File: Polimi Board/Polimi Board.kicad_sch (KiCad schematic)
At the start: 15 parts, among them J1 Conn_01x04_Socket, J2 USB_B_Micro, U1 STM32F205RCTx, U2 FT2232D, U3 LAN8742A, Y1 8MHz

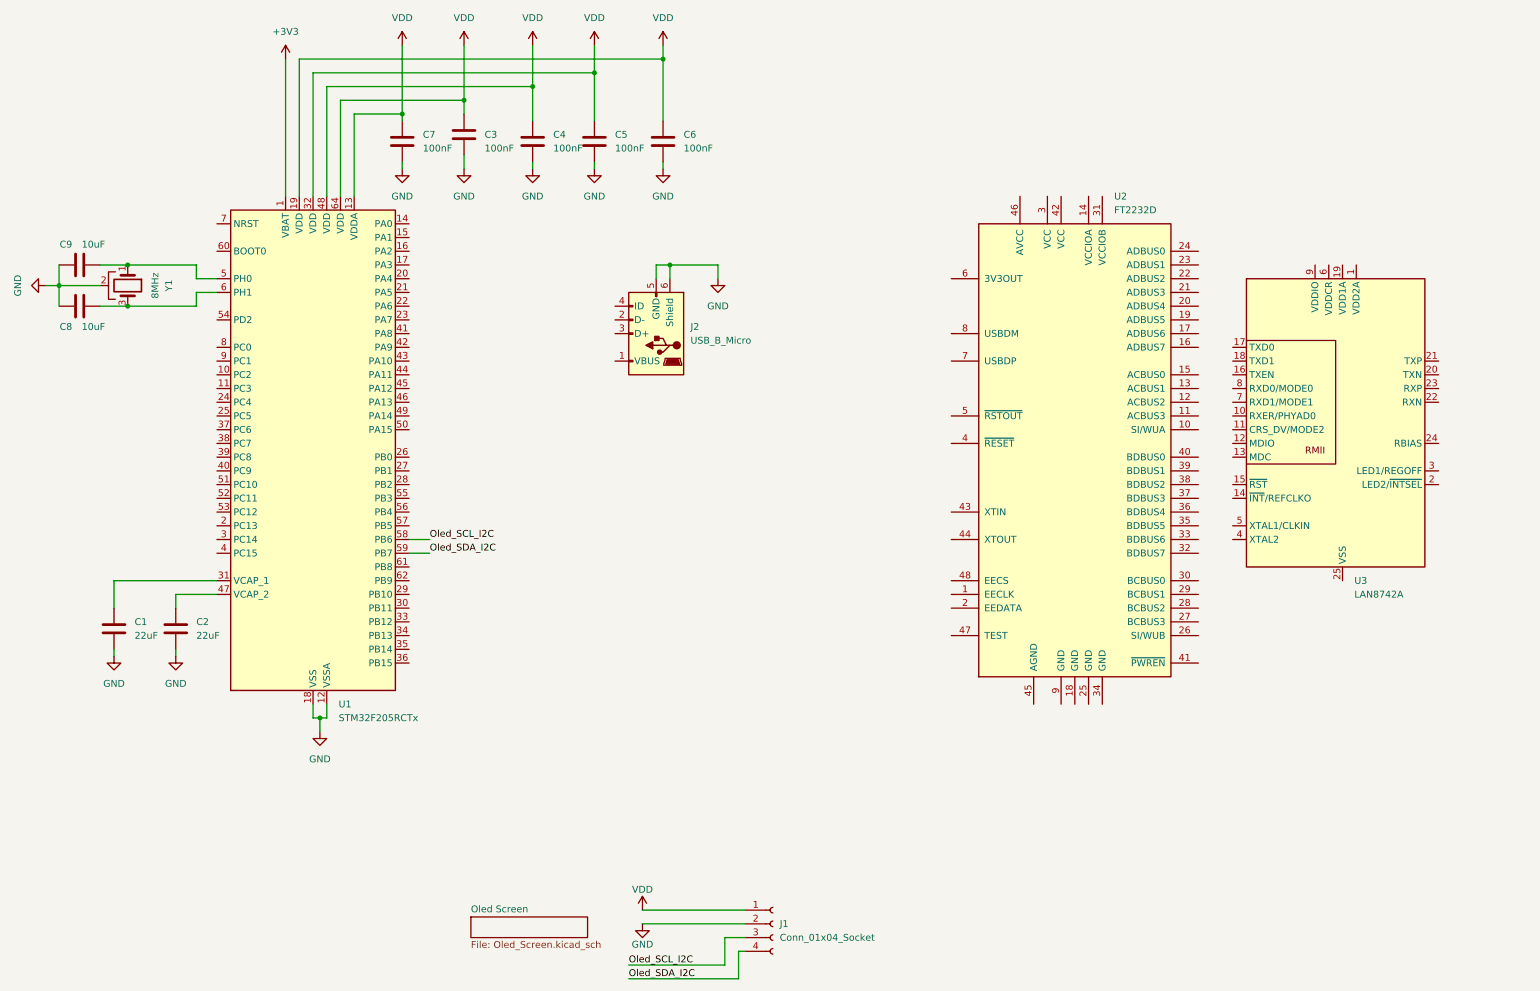
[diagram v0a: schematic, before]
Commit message: added programming oled and SD
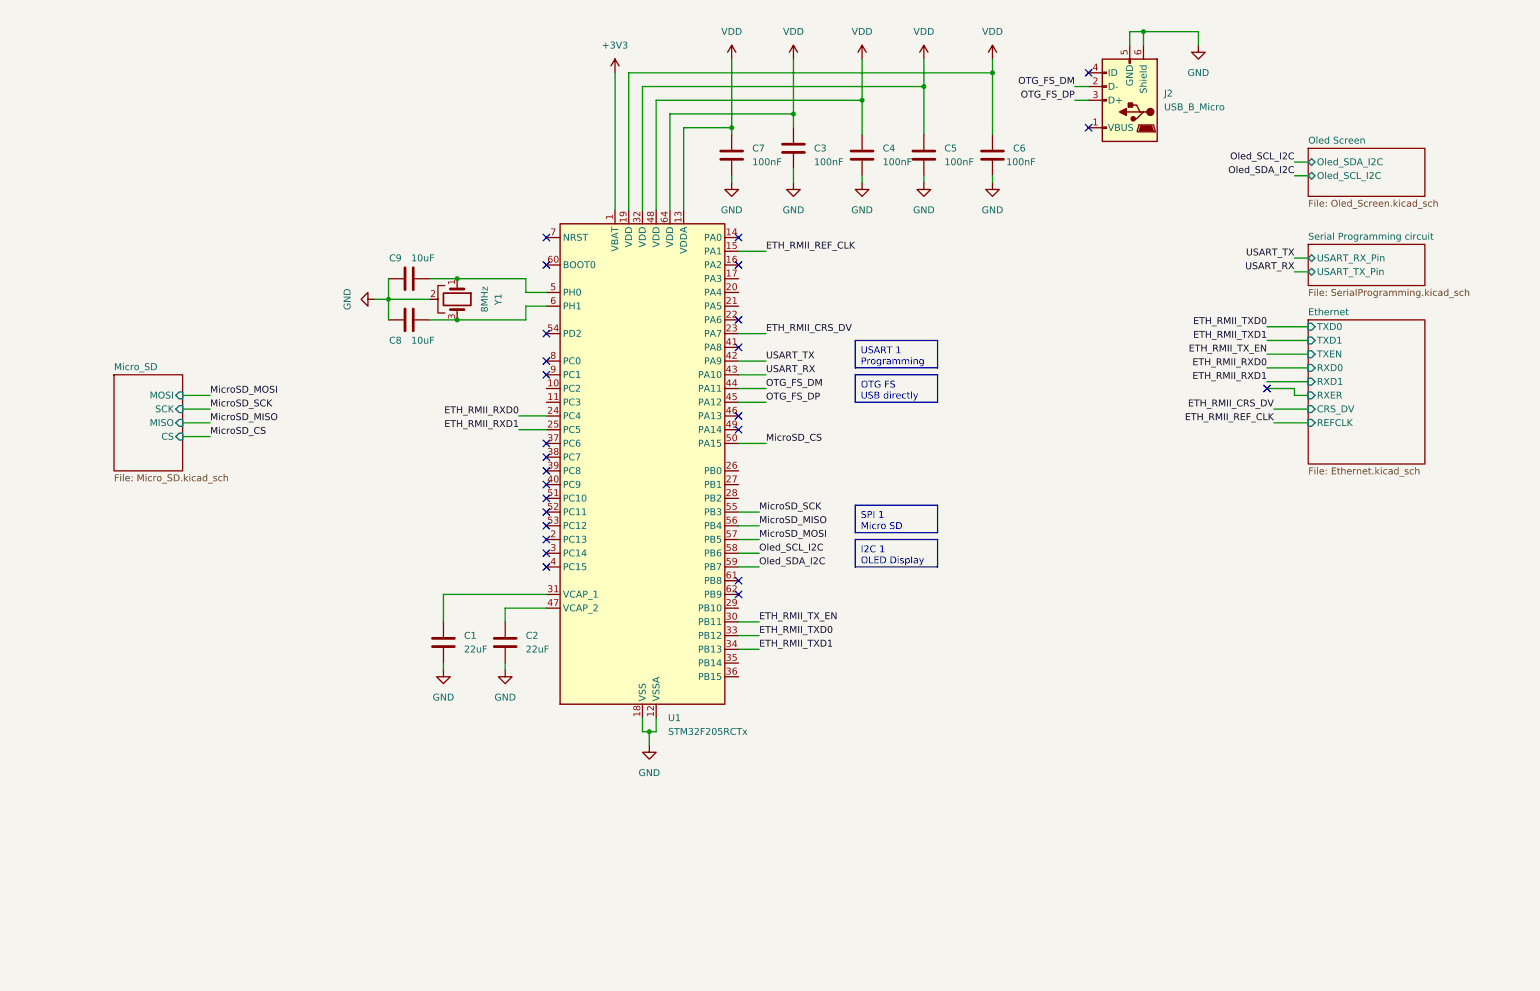
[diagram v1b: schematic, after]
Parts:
- removed J1: Conn_01x04_Socket, symbol Connector:Conn_01x04_Socket
- removed U2: FT2232D, Package_QFP:LQFP-48_7x7mm_P0.5mm, symbol Interface_USB:FT2232D
- removed U3: LAN8742A, Package_DFN_QFN:VQFN-24-1EP_4x4mm_P0.5mm_EP2.5x2.5mm_ThermalVias, symbol Interface_Ethernet:LAN8742A
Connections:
- net OTG_FS_DM: now reaches J2.2 (D-)
- net OTG_FS_DM: now also U1.44 (PA11)
- net OTG_FS_DP: now reaches J2.3 (D+)
- net OTG_FS_DP: now also U1.45 (PA12)
- net ETH_RMII_REF_CLK: now reaches U1.15 (PA1)
- net ETH_RMII_CRS_DV: now reaches U1.23 (PA7)
- net ETH_RMII_RXD0: now reaches U1.24 (PC4)
- net ETH_RMII_RXD1: now reaches U1.25 (PC5)
- net ETH_RMII_TX_EN: now reaches U1.30 (PB11)
- net ETH_RMII_TXD0: now reaches U1.33 (PB12)
- net ETH_RMII_TXD1: now reaches U1.34 (PB13)
- net USART_TX: now reaches U1.42 (PA9)
- net USART_RX: now reaches U1.43 (PA10)
- net MicroSD_CS: now reaches U1.50 (PA15)
- net MicroSD_SCK: now reaches U1.55 (PB3)
- net MicroSD_MISO: now reaches U1.56 (PB4)
- net MicroSD_MOSI: now reaches U1.57 (PB5)
- no-connect marks 0 -> 26
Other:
- added sheet Ethernet (Ethernet.kicad_sch)
- added sheet Micro_SD (Micro_SD.kicad_sch)
- added sheet Serial Programming circuit (SerialProgramming.kicad_sch)
- sheet Oled Screen ports: added Oled_SCL_I2C, Oled_SDA_I2C; removed none
- title: Polimi Board - Embedded Systems project -> Polimi Board 
- moved on the sheet: C1, C2, C3, C4, C5, C6, C7, C8, C9, J2, U1, Y1

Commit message: Added GPIOs
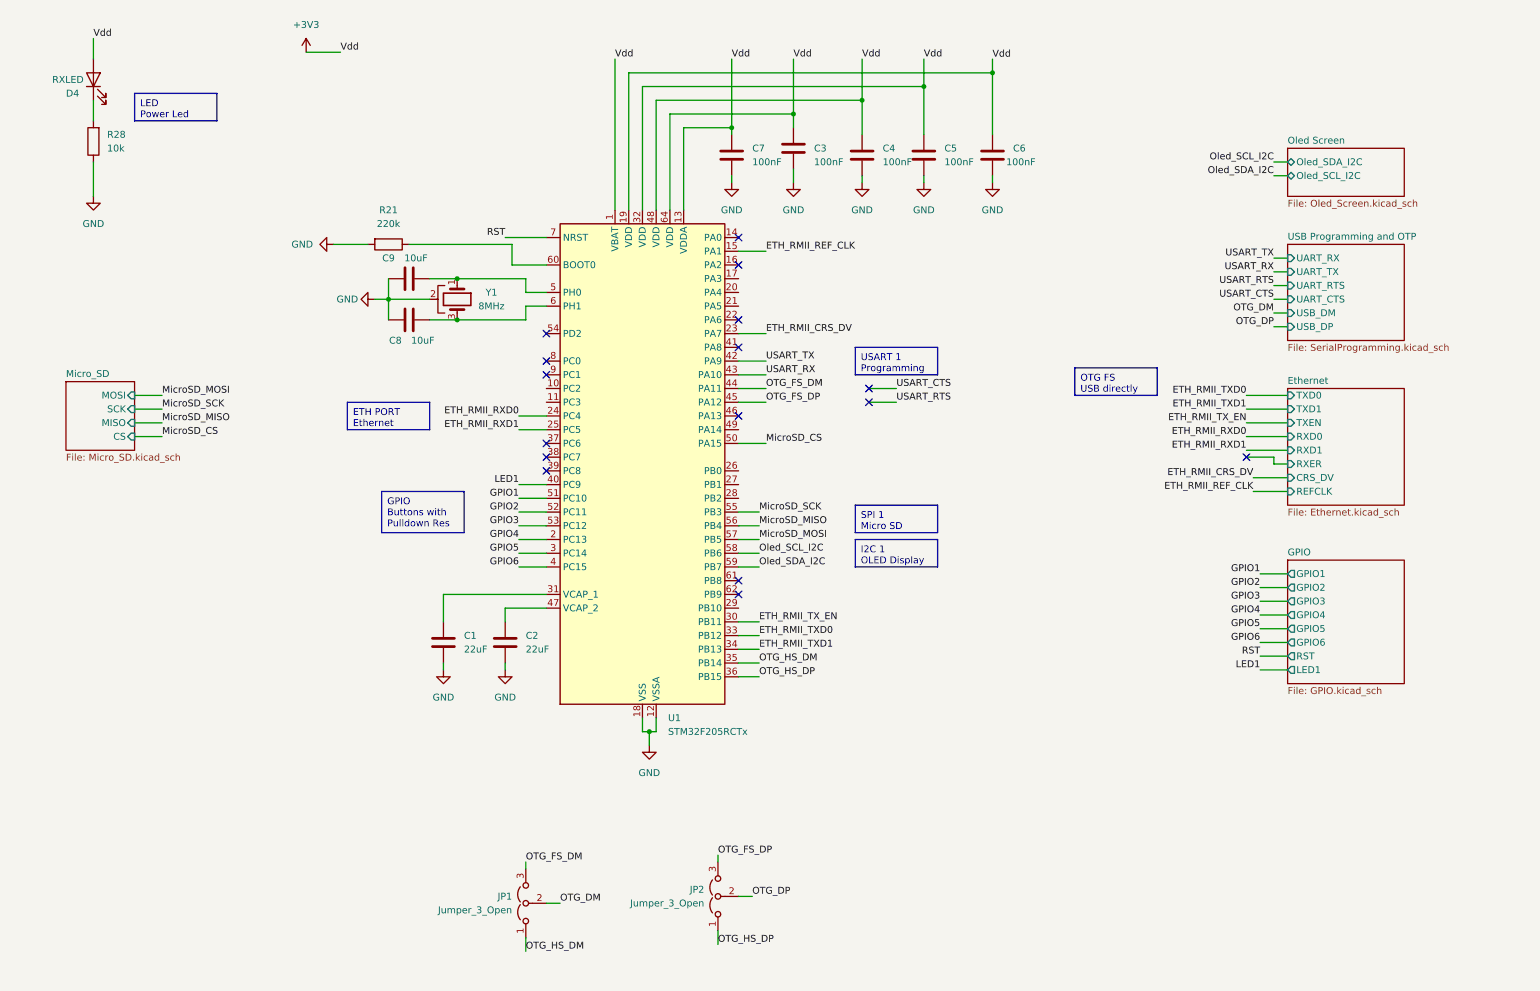
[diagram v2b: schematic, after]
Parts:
- removed J2: USB_B_Micro, symbol Connector:USB_B_Micro
- added D4: RXLED, symbol Device:LED
- added JP1, JP2: Jumper_3_Open, symbol Jumper:Jumper_3_Open
- added R21: 220k, symbol Device:R
- added R28: 10k, symbol Device:R
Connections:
- net VDD is gone; now on net +3V3: C3.1, C4.1, C5.1, C6.1, C7.1, U1.13 (VDDA), U1.19 (VDD), U1.32 (VDD), U1.48 (VDD), U1.64 (VDD)
- net +3V3: now also D4.2 (A)
- net GND: now also R21.2, R28.1
- net OTG_FS_DM: now also JP1.3 (B)
- net OTG_FS_DP: now also JP2.3 (B)
- net GPIO4: now reaches U1.2 (PC13)
- net GPIO5: now reaches U1.3 (PC14)
- net OTG_HS_DM: now reaches U1.35 (PB14)
- net OTG_HS_DM: now also JP1.1 (A)
- net OTG_HS_DP: now reaches U1.36 (PB15)
- net OTG_HS_DP: now also JP2.1 (A)
- net GPIO6: now reaches U1.4 (PC15)
- net LED1: now reaches U1.40 (PC9)
- net GPIO1: now reaches U1.51 (PC10)
- net GPIO2: now reaches U1.52 (PC11)
- net GPIO3: now reaches U1.53 (PC12)
- net at U1.60 (BOOT0): now also R21.1
- net RST: now reaches U1.7 (NRST)
- new net: D4.1 (K), R28.2
- new net OTG_DM: JP1.2 (C)
- new net OTG_DP: JP2.2 (C)
- no-connect marks 26 -> 16
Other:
- sheet Serial Programming circuit renamed USB Programming and OTP
- added sheet GPIO (GPIO.kicad_sch)
- sheet USB Programming and OTP ports: added UART_CTS, UART_RTS, UART_RX, UART_TX, USB_DM, USB_DP; removed USART_RX_Pin, USART_TX_Pin

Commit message: Finish schematic part
To be reviewd
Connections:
- net GPIO1: now also U1.38 (PC7); no longer U1.51 (PC10)
- net GPIO2: now also U1.39 (PC8); no longer U1.52 (PC11)
- net GPIO3: now also U1.40 (PC9); no longer U1.53 (PC12)
- net LED1: now also U1.37 (PC6); no longer U1.40 (PC9)
- net Flash_CS: now reaches U1.20 (PA4)
- net +3V3 renamed +3.3V
- net +3.3V: no longer D4.2 (A)
- new net +5V: D4.2 (A)
- new net Flash_MISO: U1.52 (PC11)
- new net Flash_MOSI: U1.53 (PC12)
- new net Flash_SCK: U1.51 (PC10)
- no-connect marks 16 -> 22
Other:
- added sheet External Flash SPI (SPI Flash.kicad_sch)
- added sheet Power (Power.kicad_sch)
- sheet Oled Screen ports: added Vdd, gnd; removed none
- moved on the sheet: D4, JP1, JP2

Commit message: Fatte modifiche
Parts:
- added SW8: SW_Push, symbol Switch:SW_Push
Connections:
- net MicroSD_MISO is gone; now on net Flash_MISO: U1.56 (PB4)
- net MicroSD_MOSI is gone; now on net Flash_MOSI: U1.57 (PB5)
- net MicroSD_SCK is gone; now on net Flash_SCK: U1.55 (PB3)
- net +3.3V: now also SW8.2
- net Flash_MISO: no longer U1.52 (PC11)
- net Flash_MOSI: no longer U1.53 (PC12)
- net Flash_SCK: no longer U1.51 (PC10)
- net GPIO1: now also U1.9 (PC1); no longer U1.38 (PC7)
- net GPIO2: now also U1.10 (PC2); no longer U1.39 (PC8)
- net GPIO3: now also U1.11 (PC3); no longer U1.40 (PC9)
- net LED1: now also U1.8 (PC0); no longer U1.37 (PC6)
- net SDMMC_CMD: now reaches U1.54 (PD2)
- net at R21.1, U1.60 (BOOT0): now also SW8.1
- net MicroSD_CS: no longer names the net of U1.50 (PA15)
- new net SDMMC_CD: U1.37 (PC6)
- new net SDMMC_CK: U1.53 (PC12)
- new net SDMMC_D0: U1.39 (PC8)
- new net SDMMC_D1: U1.40 (PC9)
- new net SDMMC_D2: U1.51 (PC10)
- new net SDMMC_D3: U1.52 (PC11)
- new net SDMMC_WP: U1.38 (PC7)
- no-connect marks 22 -> 18
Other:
- sheet Micro_SD ports: added SDMMC_CD, SDMMC_CK, SDMMC_CMD, SDMMC_D0, SDMMC_D1, SDMMC_D2, SDMMC_D3, SDMMC_WP; removed CS, MISO, MOSI, SCK
- sheet Oled Screen ports: added none; removed Vdd, gnd
- note added: "TX and RX are swapped here"
- moved on the sheet: C1, C2, C3, C4, C5, C6, C7, C8, C9, R21, U1, Y1

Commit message: Update the design with new specifications
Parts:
- Y1: value 8MHz -> 25MHz
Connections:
- net Flash_MISO: now also U1.22 (PA6); no longer U1.56 (PB4)
- net Flash_SCK: now also U1.21 (PA5); no longer U1.55 (PB3)
- net MCO: now reaches U1.41 (PA8)
- net JTAG_TMS: now reaches U1.46 (PA13)
- net JTAG_TCK: now reaches U1.49 (PA14)
- net JTAG_TDI: now reaches U1.50 (PA15)
- new net JTAG_TD0: U1.55 (PB3)
- new net JTAG_TRST: U1.56 (PB4)
- no-connect marks 18 -> 12
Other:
- sheet Ethernet ports: added MCO; removed none
- sheet Power ports: added none; removed Vdd_out_3V3, Vdd_out_5V
- note added: "Power section"
- moved on the sheet: D4, R28

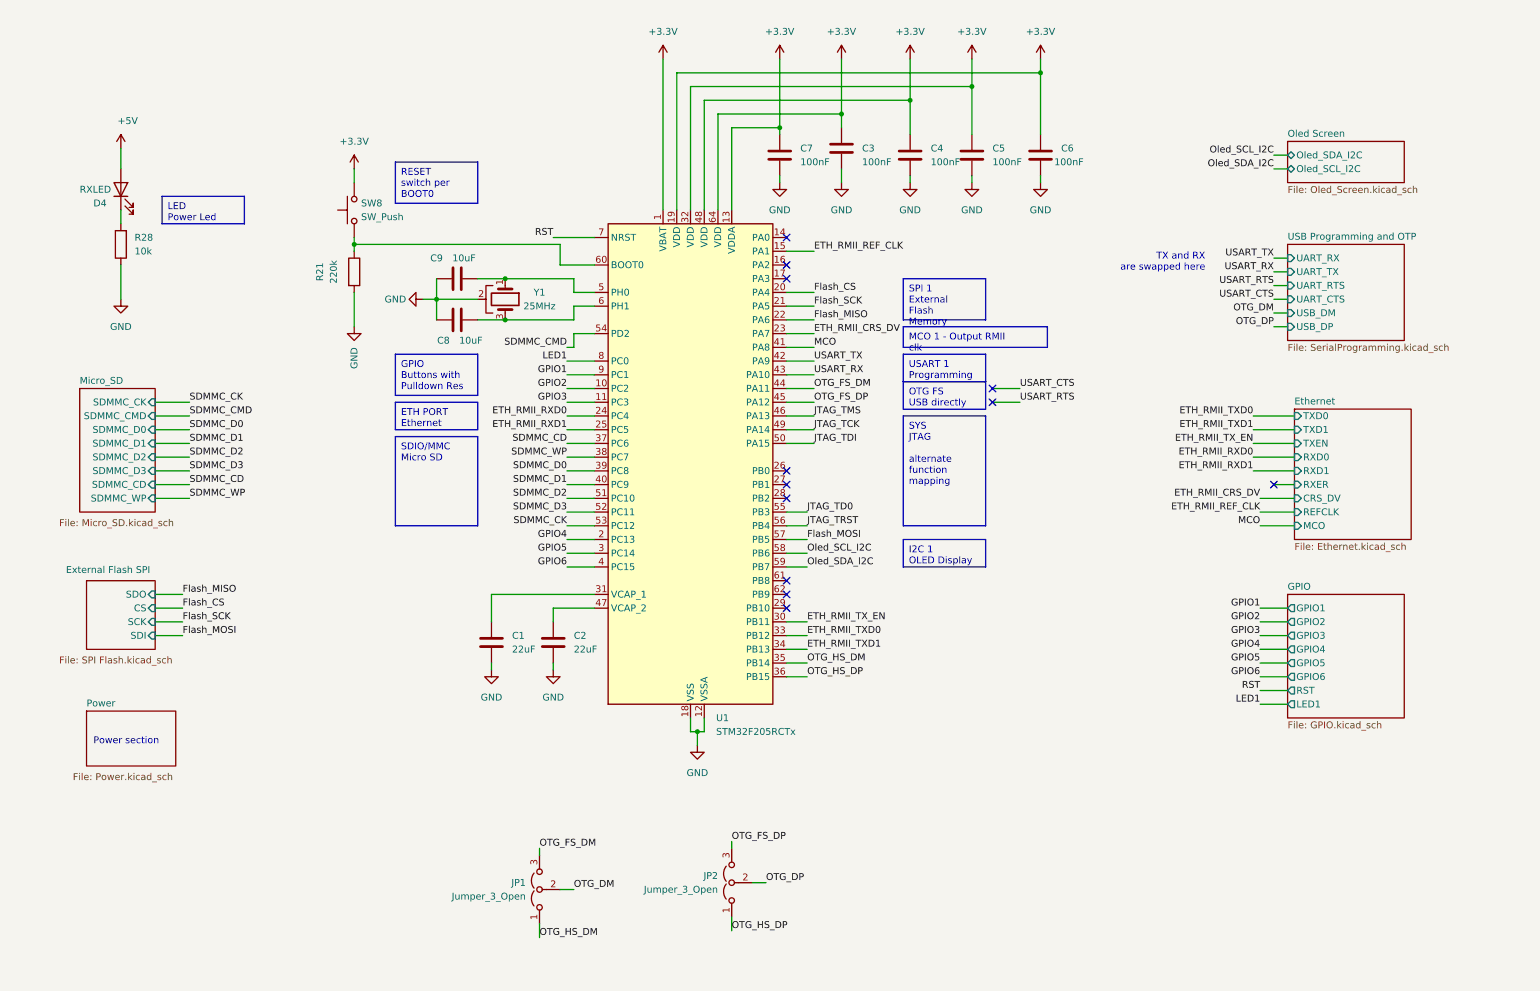
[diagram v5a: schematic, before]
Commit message: Update resets and readme
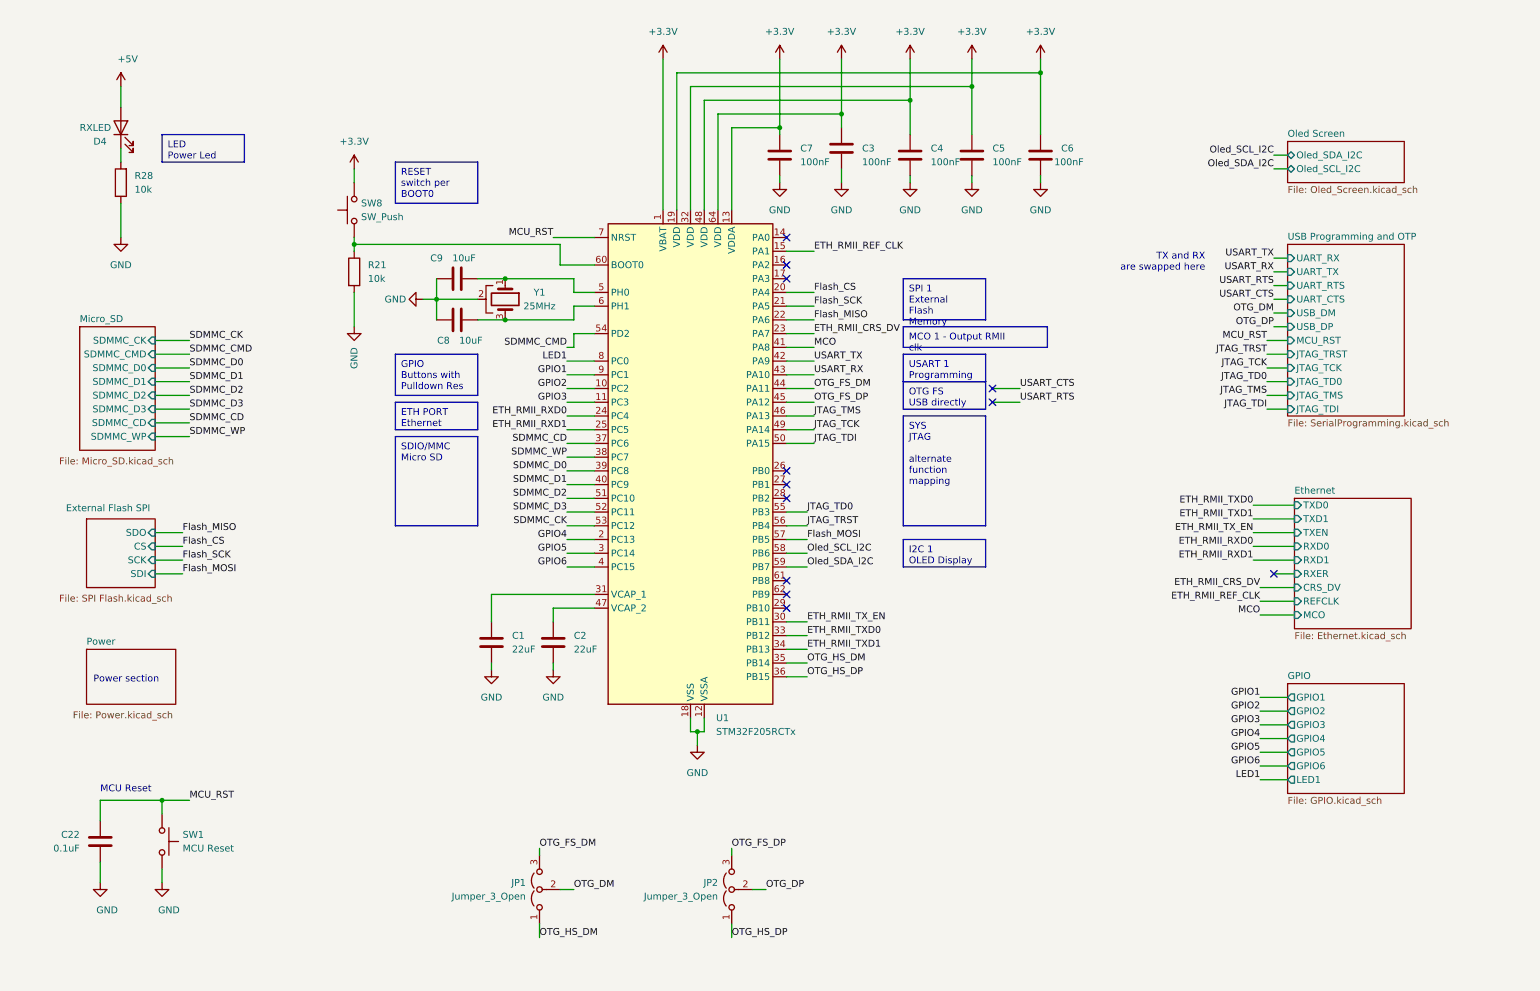
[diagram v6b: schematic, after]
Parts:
- added C22: 0.1uF, symbol Device:C
- added SW1: MCU Reset, symbol Switch:SW_Push
- R21: value 220k -> 10k
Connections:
- net GND: now also C22.2, SW1.1
- net RST renamed MCU_RST
- net MCU_RST: now also C22.1, SW1.2
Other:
- sheet GPIO ports: added none; removed RST
- sheet USB Programming and OTP ports: added JTAG_TCK, JTAG_TD0, JTAG_TDI, JTAG_TMS, JTAG_TRST, MCU_RST; removed none
- note added: "MCU Reset"
- moved on the sheet: D4, JP2, R28
